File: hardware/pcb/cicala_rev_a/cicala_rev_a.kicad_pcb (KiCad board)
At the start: 4 copper layers, 78 x 45 mm, 0 parts

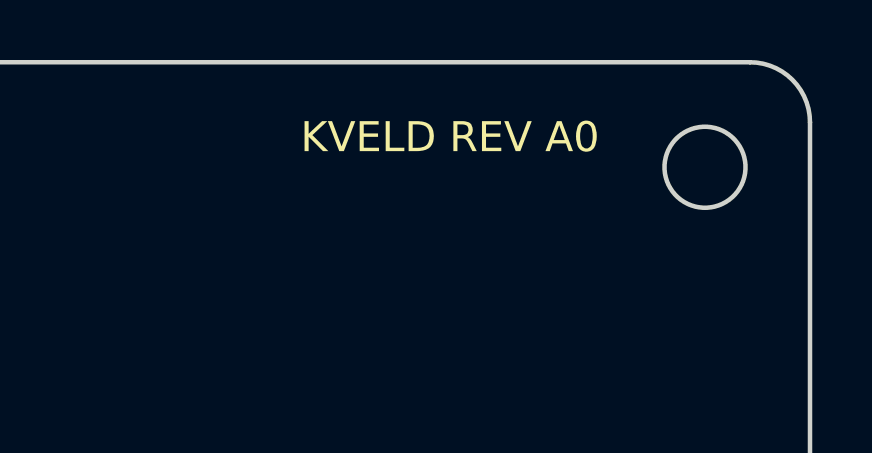
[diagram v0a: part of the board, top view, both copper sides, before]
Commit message: feat: rename project and adopt Cicala identity
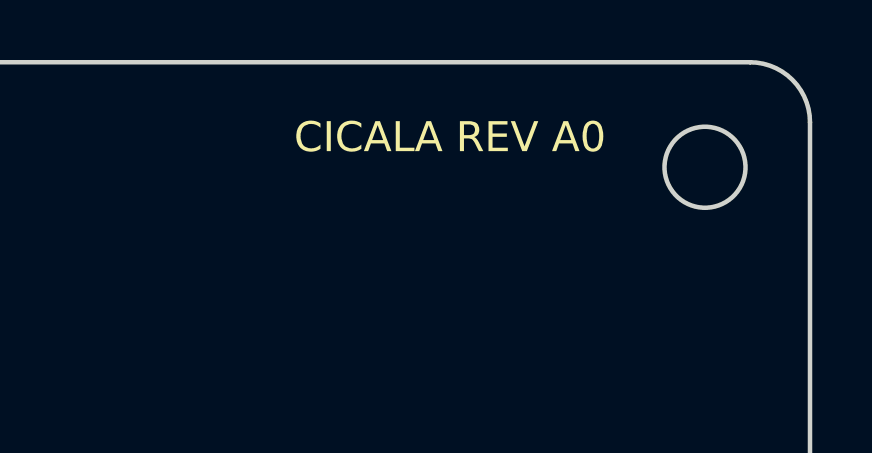
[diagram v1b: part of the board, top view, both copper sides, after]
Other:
- board text added: "CICALA REV A0"
- board text removed: "KVELD REV A0"
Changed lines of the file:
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@@
 	(paper "A4")
 	(title_block
-		(title "Kveld Rev A constraint skeleton")
+		(title "Cicala Rev A constraint skeleton")
 		(date "2026-08-16")
 		(rev "A0")
-		(company "Kveld")
+		(company "Cicala")
 		(comment 1 "NOT FABRICATION READY — mechanical and placement contract only")
 	)
@@
 	(gr_text "DISPLAY ENVELOPE ABOVE" (at 42 35 0) (layer "User.1") (effects (font (size 1 1) (thickness 0.15))))
 	(gr_text "USB-C" (at 42 46 0) (layer "F.SilkS") (effects (font (size 0.8 0.8) (thickness 0.12))))
-	(gr_text "KVELD REV A0" (at 69 5.5 0) (layer "F.SilkS") (effects (font (size 1 1) (thickness 0.15))))
+	(gr_text "CICALA REV A0" (at 69 5.5 0) (layer "F.SilkS") (effects (font (size 1 1) (thickness 0.15))))
 	(gr_text "FPC DATUM — VERIFY FOOTPRINT" (at 42 40 0) (layer "User.1") (effects (font (size 0.65 0.65) (thickness 0.1))))
 	(gr_text "WROOM-1 CONFLICT / 1U BASELINE" (at 16 28 90) (layer "Cmts.User") (effects (font (size 0.55 0.55) (thickness 0.09))))
